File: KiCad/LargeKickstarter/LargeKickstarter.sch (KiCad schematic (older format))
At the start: 299 parts, among them P1 CONN_01X03, P2 CONN_01X02, P4 CONN_02X03, SW1 HOUR, SW2 MIN, SW4 SOFT, SW6 RST, U1 HT16K33, U2 DS3231, U3 ATMEGA328-TQFP, U4 HT16K33

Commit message: Full Redesign
Doubled LED count. Added footprints for modules. Still need DS3231
module added.
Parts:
- removed R8: 10K, Resistors_SMD:R_0603_HandSoldering, symbol R
- removed SW6: RST, SparkFun-Electromechanical:TACTILE-PTH-SIDEEZ, symbol SW_PUSH
- added 0-16, 0-17, 0-18, 0-19, 0-20, 0-21, 0-22, 0-23, 0-24, 0-25, 0-26, 0-27, 0-28, 0-29, 0-30, 0-31, 1-16, 1-17, 1-18, 1-19, 1-20, 1-21, 1-22, 1-23, 1-24, 1-25, 1-26, 1-27, 1-28, 1-29, 1-30, 1-31, 10-16, 10-17, 10-18, 10-19, 10-20, 10-21, 10-22, 10-23, 10-24, 10-25, 10-26, 10-27, 10-28, 10-29, 10-30, 10-31, 11-16, 11-17, 11-18, 11-19, 11-20, 11-21, 11-22, 11-23, 11-24, 11-25, 11-26, 11-27, 11-28, 11-29, 11-30, 11-31, 12-16, 12-17, 12-18, 12-19, 12-20, 12-21, 12-22, 12-23, 12-24, 12-25, 12-26, 12-27, 12-28, 12-29, 12-30, 12-31, 13-16, 13-17, 13-18, 13-19, 13-20, 13-21, 13-22, 13-23, 13-24, 13-25, 13-26, 13-27, 13-28, 13-29, 13-30, 13-31, 14-16, 14-17, 14-18, 14-19, 14-20, 14-21, 14-22, 14-23, 14-24, 14-25, 14-26, 14-27, 14-28, 14-29, 14-30, 14-31, 15-16, 15-17, 15-18, 15-19, 15-20, 15-21, 15-22, 15-23, 15-24, 15-25, 15-26, 15-27, 15-28, 15-29, 15-30, 15-31, 2-16, 2-17, 2-18, 2-19, 2-20, 2-21, 2-22, 2-23, 2-24, 2-25, 2-26, 2-27, 2-28, 2-29, 2-30, 2-31, 3-16, 3-17, 3-18, 3-19, 3-20, 3-21, 3-22, 3-23, 3-24, 3-25, 3-26, 3-27, 3-28, 3-29, 3-30, 3-31, 4-16, 4-17, 4-18, 4-19, 4-20, 4-21, 4-22, 4-23, 4-24, 4-25, 4-26, 4-27, 4-28, 4-29, 4-30, 4-31, 5-16, 5-17, 5-18, 5-19, 5-20, 5-21, 5-22, 5-23, 5-24, 5-25, 5-26, 5-27, 5-28, 5-29, 5-30, 5-31, 6-16, 6-17, 6-18, 6-19, 6-20, 6-21, 6-22, 6-23, 6-24, 6-25, 6-26, 6-27, 6-28, 6-29, 6-30, 6-31, 7-16, 7-17, 7-18, 7-19, 7-20, 7-21, 7-22, 7-23, 7-24, 7-25, 7-26, 7-27, 7-28, 7-29, 7-30, 7-31, 8-16, 8-17, 8-18, 8-19, 8-20, 8-21, 8-22, 8-23, 8-24, 8-25, 8-26, 8-27, 8-28, 8-29, 8-30, 8-31, 9-16, 9-17, 9-18, 9-19, 9-20, 9-21, 9-22, 9-23, 9-24, 9-25, 9-26, 9-27, 9-28, 9-29, 9-30, 9-31: LED, LikeClockwork:SMD_LED_PLCC_2, symbol LED
- added C7, C8: 0.1uF, Capacitors_SMD:C_0603_HandSoldering, symbol CP2
- added D4, D5: DIODE, Diodes_SMD:SOD-323, symbol DIODE
- added JP10, JP11, JP12, JP7, JP8, JP9: JUMPER, LikeClockwork:solder_jumper, symbol JUMPER
- added R12, R13, R14, R15, R16, R17: 47K, Resistors_SMD:R_0603_HandSoldering, symbol R
- added U10, U12: HT16K33, adafruit:SO28W, symbol HT16K33
- added U11, U9: HT16K33_BOUT, LikeClockwork:HT16K33_Breakout, symbol HT16K33_BOUT
- JP1, JP2, JP3, JP4, JP5, JP6: renamed from JP?; footprint (none) -> LikeClockwork:solder_jumper
- U5, U6: renamed from U?; footprint MODULE -> LikeClockwork:HT16K33_Breakout
- U7: renamed from U?; footprint MODULE -> LikeClockwork:Arduino_Nano
- U8: renamed from U?; footprint MODULE -> LikeClockwork:shield_footprint
- gave numbers to parts that had none: 7
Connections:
- net labels added: COM-2-0, COM-2-1, COM-2-2, COM-2-3, COM-2-4, COM-2-5, COM-2-6, COM-2-7, COM-3-0, COM-3-1, COM-3-2, COM-3-3, COM-3-4, COM-3-5, COM-3-6, COM-3-7, RAW, ROW-2-0, ROW-2-1, ROW-2-10, ROW-2-11, ROW-2-12, ROW-2-13, ROW-2-14, ROW-2-15, ROW-2-2, ROW-2-3, ROW-2-4, ROW-2-5, ROW-2-6, ROW-2-7, ROW-2-8, ROW-2-9, ROW-3-0, ROW-3-1, ROW-3-10, ROW-3-11, ROW-3-12, ROW-3-13, ROW-3-14, ROW-3-15, ROW-3-2, ROW-3-3, ROW-3-4, ROW-3-5, ROW-3-6, ROW-3-7, ROW-3-8, ROW-3-9
- net labels removed: Vin1, Vin2
- wire segments 647 -> 1157
- no-connect marks 9 -> 7
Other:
- moved on the sheet: 0-0, 0-1, 0-2, 0-3, 0-4, 0-5, 0-6, 0-7, 1-0, 1-1, 1-2, 1-3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

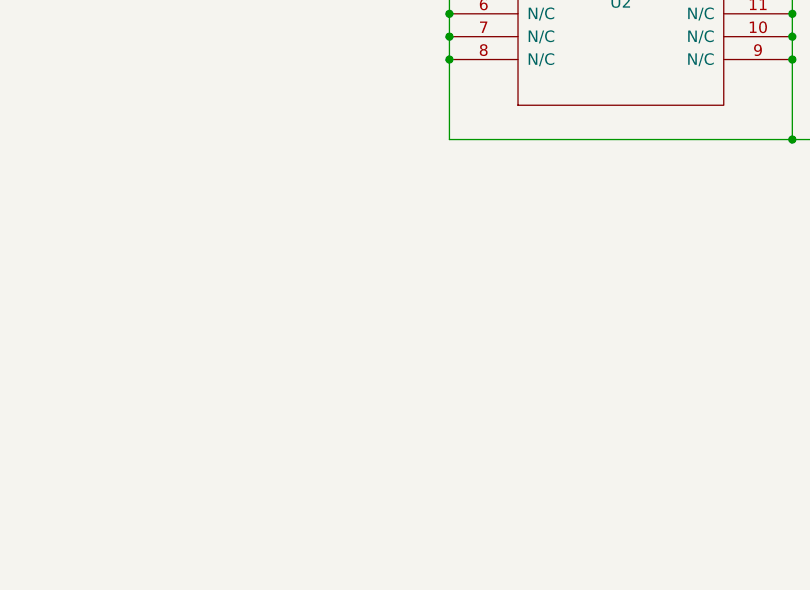
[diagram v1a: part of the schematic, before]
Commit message: Added DS3231 module footprints
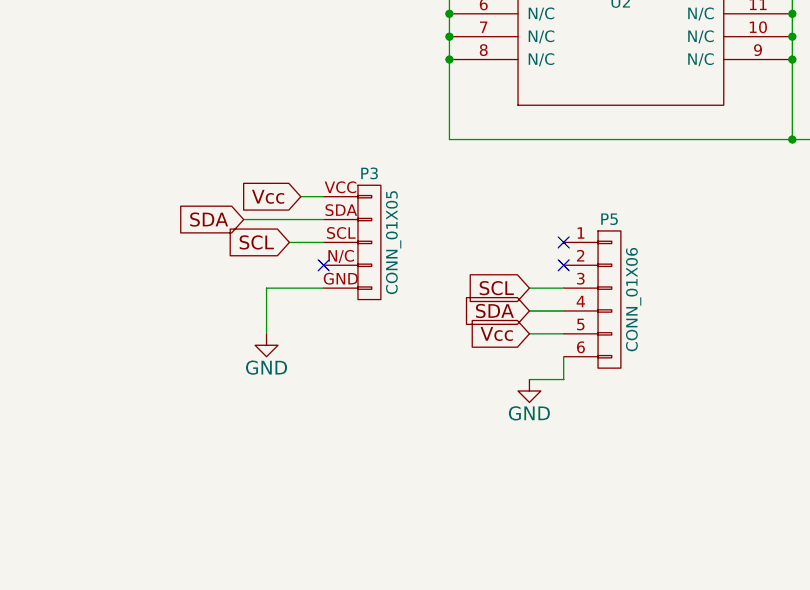
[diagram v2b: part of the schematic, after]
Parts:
- added P3: CONN_01X05, Pin_Headers:Pin_Header_Straight_1x05, symbol CONN_01X05
- added P5: CONN_01X06, Pin_Headers:Pin_Header_Straight_1x06, symbol CONN_01X06
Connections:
- net GND: now also P3.GND (P5), P5.6 (P6)
- net SCL: now also P3.SCL, P5.3 (P3)
- net SDA: now also P3.SDA, P5.4 (P4)
- net Vcc: now also P3.VCC, P5.5 (P5)
- no-connect marks 7 -> 10

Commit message: Schematic Tweaks
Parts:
- added D6: DIODE, Diodes_ThroughHole:Diode_DO-41_SOD81_Horizontal_RM10, symbol DIODE
- added R18, R19, R20: 10K, Resistors_ThroughHole:Resistor_Horizontal_RM10mm, symbol R-RESCUE-LargeKickstarter
- 0-0, 0-1, 0-10, 0-11, 0-12, 0-13, 0-14, 0-15, 0-16, 0-17, 0-18, 0-19, 0-2, 0-20, 0-21, 0-22, 0-23, 0-24, 0-25, 0-26, 0-27, 0-28, 0-29, 0-3, 0-30, 0-31, 0-4, 0-5, 0-6, 0-7, 0-8, 0-9, 1-0, 1-1, 1-10, 1-11, 1-12, 1-13, 1-14, 1-15, 1-16, 1-17, 1-18, 1-19, 1-2, 1-20, 1-21, 1-22, 1-23, 1-24, 1-25, 1-26, 1-27, 1-28, 1-29, 1-3, 1-30, 1-31, 1-4, 1-5, 1-6, 1-7, 1-8, 1-9, 10-0, 10-1, 10-10, 10-11, 10-12, 10-13, 10-14, 10-15, 10-16, 10-17, 10-18, 10-19, 10-2, 10-20, 10-21, 10-22, 10-23, 10-24, 10-25, 10-26, 10-27, 10-28, 10-29, 10-3, 10-30, 10-31, 10-4, 10-5, 10-6, 10-7, 10-8, 10-9, 11-0, 11-1, 11-10, 11-11, 11-12, 11-13, 11-14, 11-15, 11-16, 11-17, 11-18, 11-19, 11-2, 11-20, 11-21, 11-22, 11-23, 11-24, 11-25, 11-26, 11-27, 11-28, 11-29, 11-3, 11-30, 11-31, 11-4, 11-5, 11-6, 11-7, 11-8, 11-9, 12-0, 12-1, 12-10, 12-11, 12-12, 12-13, 12-14, 12-15, 12-16, 12-17, 12-18, 12-19, 12-2, 12-20, 12-21, 12-22, 12-23, 12-24, 12-25, 12-26, 12-27, 12-28, 12-29, 12-3, 12-30, 12-31, 12-4, 12-5, 12-6, 12-7, 12-8, 12-9, 13-0, 13-1, 13-10, 13-11, 13-12, 13-13, 13-14, 13-15, 13-16, 13-17, 13-18, 13-19, 13-2, 13-20, 13-21, 13-22, 13-23, 13-24, 13-25, 13-26, 13-27, 13-28, 13-29, 13-3, 13-30, 13-31, 13-4, 13-5, 13-6, 13-7, 13-8, 13-9, 14-0, 14-1, 14-10, 14-11, 14-12, 14-13, 14-14, 14-15, 14-16, 14-17, 14-18, 14-19, 14-2, 14-20, 14-21, 14-22, 14-23, 14-24, 14-25, 14-26, 14-27, 14-28, 14-29, 14-3, 14-30, 14-31, 14-4, 14-5, 14-6, 14-7, 14-8, 14-9, 15-0, 15-1, 15-10, 15-11, 15-12, 15-13, 15-14, 15-15, 15-16, 15-17, 15-18, 15-19, 15-2, 15-20, 15-21, 15-22, 15-23, 15-24, 15-25, 15-26, 15-27, 15-28, 15-29, 15-3, 15-30, 15-31, 15-4, 15-5, 15-6, 15-7, 15-8, 15-9, 2-0, 2-1, 2-10, 2-11, 2-12, 2-13, 2-14, 2-15, 2-16, 2-17, 2-18, 2-19, 2-2, 2-20, 2-21, 2-22, 2-23, 2-24, 2-25, 2-26, 2-27, 2-28, 2-29, 2-3, 2-30, 2-31, 2-4, 2-5, 2-6, 2-7, 2-8, 2-9, 3-0, 3-1, 3-10, 3-11, 3-12, 3-13, 3-14, 3-15, 3-16, 3-17, 3-18, 3-19, 3-2, 3-20, 3-21, 3-22, 3-23, 3-24, 3-25, 3-26, 3-27, 3-28, 3-29, 3-3, 3-30, 3-31, 3-4, 3-5, 3-6, 3-7, 3-8, 3-9, 4-0, 4-1, 4-10, 4-11, 4-12, 4-13, 4-14, 4-15, 4-16, 4-17, 4-18, 4-19, 4-2, 4-20, 4-21, 4-22, 4-23, 4-24, 4-25, 4-26, 4-27, 4-28, 4-29, 4-3, 4-30, 4-31, 4-4, 4-5, 4-6, 4-7, 4-8, 4-9, 5-0, 5-1, 5-10, 5-11, 5-12, 5-13, 5-14, 5-15, 5-16, 5-17, 5-18, 5-19, 5-2, 5-20, 5-21, 5-22, 5-23, 5-24, 5-25, 5-26, 5-27, 5-28, 5-29, 5-3, 5-30, 5-31, 5-4, 5-5, 5-6, 5-7, 5-8, 5-9, 6-0, 6-1, 6-10, 6-11, 6-12, 6-13, 6-14, 6-15, 6-16, 6-17, 6-18, 6-19, 6-2, 6-20, 6-21, 6-22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: symbol LED -> LED-RESCUE-LargeKickstarter
- P3: symbol CONN_01X05 -> CONN_01X05-RESCUE-LargeKickstarter
- R1, R10, R11, R12, R13, R14, R15, R16, R17, R2, R3, R4, R5, R6, R7, R8, R9: symbol R -> R-RESCUE-LargeKickstarter
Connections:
- net 5: now also R18.1
- net 6: now also R19.1
- net 7: now also R20.1
- net GND: now also R18.2, R19.2, R20.2
- net RAW: now also D6.2 (A)
- net Vin: now also D6.1 (K)

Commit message: Minor tweaks and gerber generation.
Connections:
- net VCC is gone; now on net Vcc: U3.18 (AVCC)
- net RAW renamed Vraw
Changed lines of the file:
@@
 TX
 Text GLabel 6100 5150 2    60   Input ~ 0
-VCC
+Vcc
 $Comp
 L CONN_02X03 P4
@@
 4
 Text GLabel 9400 -2800 2    60   Input ~ 0
-RAW
+Vraw
 Text GLabel 10400 -2550 0    60   Input ~ 0
 Vin
